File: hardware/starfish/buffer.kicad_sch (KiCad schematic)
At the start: 4 parts, among them U901 74HC2G34

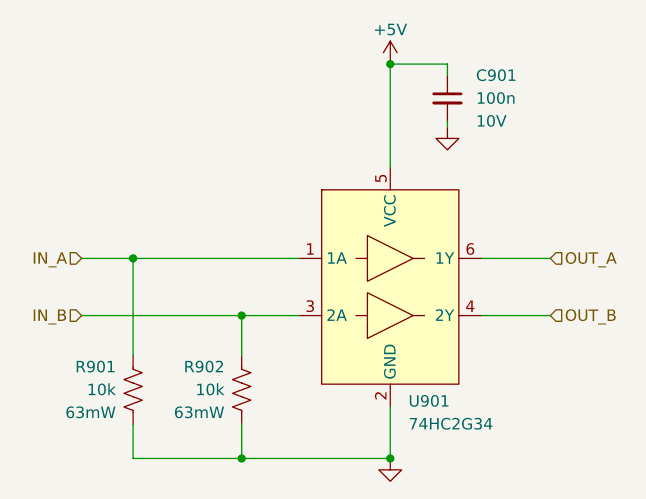
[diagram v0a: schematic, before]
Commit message: Mostly finished starfish schematic, ready for layout!
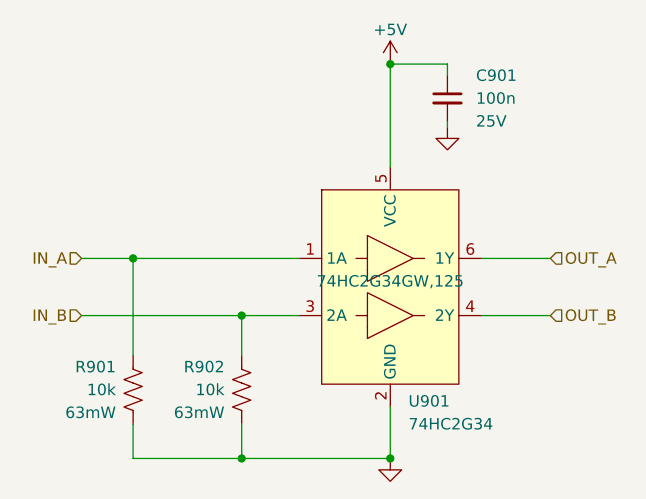
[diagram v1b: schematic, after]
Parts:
- C901: footprint Capacitor_SMD:C_0402_1005Metric_Pad0.74x0.62mm_HandSolder -> winterbloom:C_0402_HandSolder; Rating 10V -> 25V
- R901, R902: footprint Resistor_SMD:R_0402_1005Metric_Pad0.72x0.64mm_HandSolder -> winterbloom:R_0402_HandSolder
- U901: MPN (none) -> 74HC2G34GW,125
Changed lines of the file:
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@@
       (effects (font (size 1.27 1.27)) (justify left))
     )
-    (property "Footprint" "Resistor_SMD:R_0402_1005Metric_Pad0.72x0.64mm_HandSolder" (id 2) (at 110.109 110.236 90)
+    (property "Footprint" "winterbloom:R_0402_HandSolder" (id 2) (at 110.109 110.236 90)
       (effects (font (size 1.27 1.27)) hide)
     )
@@
       (effects (font (size 1.27 1.27)) (justify left) hide)
     )
+    (property "MPN" "74HC2G34GW,125" (id 5) (at 139.7 98.425 0))
     (pin "1")
     (pin "2")
@@
       (effects (font (size 1.27 1.27)) (justify left))
     )
-    (property "Footprint" "Resistor_SMD:R_0402_1005Metric_Pad0.72x0.64mm_HandSolder" (id 2) (at 122.174 110.236 90)
+    (property "Footprint" "winterbloom:R_0402_HandSolder" (id 2) (at 122.174 110.236 90)
       (effects (font (size 1.27 1.27)) hide)
     )
@@
       (effects (font (size 1.27 1.27)) (justify left))
     )
-    (property "Footprint" "Capacitor_SMD:C_0402_1005Metric_Pad0.74x0.62mm_HandSolder" (id 2) (at 146.05 78.105 0)
+    (property "Footprint" "winterbloom:C_0402_HandSolder" (id 2) (at 146.05 78.105 0)
       (effects (font (size 1.27 1.27)) hide)
     )
@@
       (effects (font (size 1.27 1.27)) hide)
     )
-    (property "Rating" "10V" (id 4) (at 149.225 80.6512 0)
+    (property "Rating" "25V" (id 4) (at 149.225 80.6512 0)
       (effects (font (size 1.27 1.27)) (justify left))
     )

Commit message: First pass at layout and routing
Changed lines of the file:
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@@
       (effects (font (size 1.27 1.27)) (justify left) hide)
     )
-    (property "MPN" "74HC2G34GW,125" (id 5) (at 139.7 98.425 0))
+    (property "MPN" "74HC2G34GW,125" (id 5) (at 139.7 98.425 0)
+      (effects (font (size 1.27 1.27)) hide)
+    )
     (pin "1")
     (pin "2")

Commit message: Run through purchasing, update some cap sizes
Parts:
- U901: MPN 74HC2G34GW,125 -> (none)
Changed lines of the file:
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@@
       (effects (font (size 1.27 1.27)) (justify left) hide)
     )
-    (property "MPN" "74HC2G34GW,125" (id 5) (at 139.7 98.425 0)
+    (property "MPN" "" (id 5) (at 139.7 98.425 0)
       (effects (font (size 1.27 1.27)) hide)
     )
